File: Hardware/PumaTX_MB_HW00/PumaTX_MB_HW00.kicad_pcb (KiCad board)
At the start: 4 copper layers, 130 x 40 mm, 115 parts, among them J100 FH12A-26S-0.5SH_55_, J101 FH12-12S-0.5SH_55_, J102 500334-0160, J103 500334-0160, J104 692122030100, J105 53398-0667, J400 U.FL-R-SMT-1_40_, J410 U.FL-R-SMT-1_40_, M130 Motor_DC, M140 Fan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

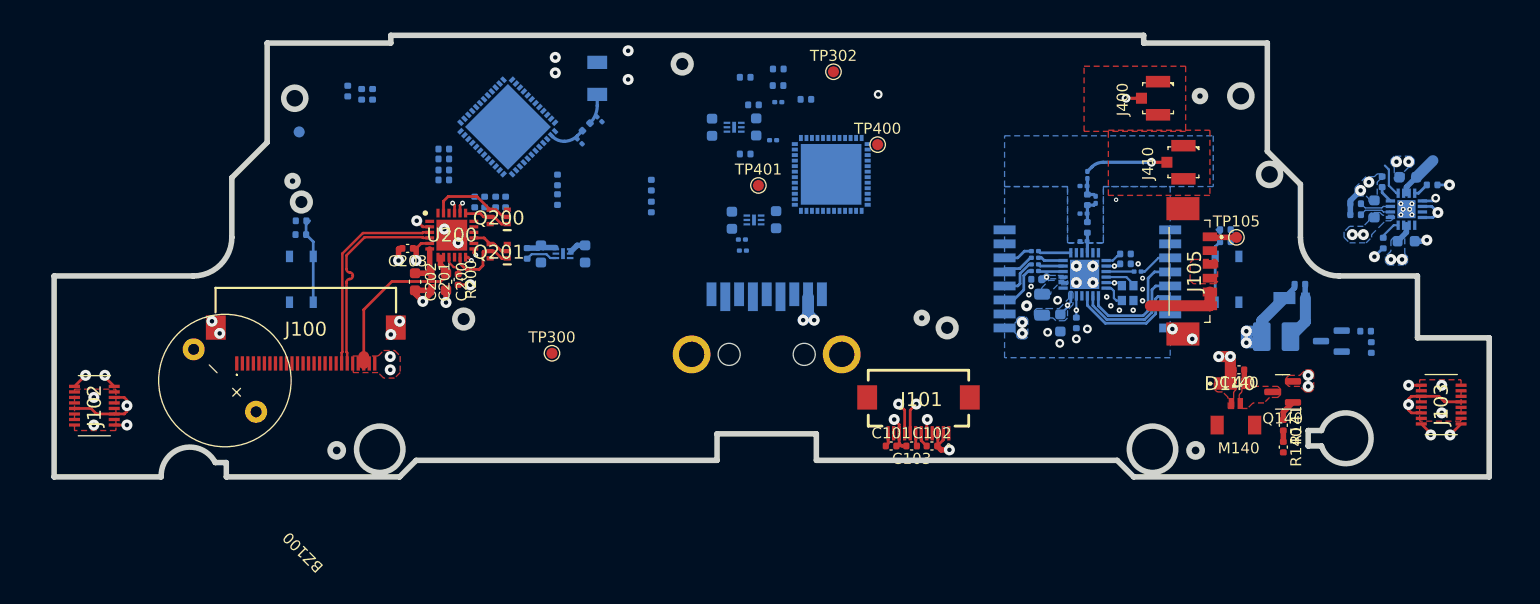
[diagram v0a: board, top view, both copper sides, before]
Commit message: some changes on routing, every QFN is on the same side
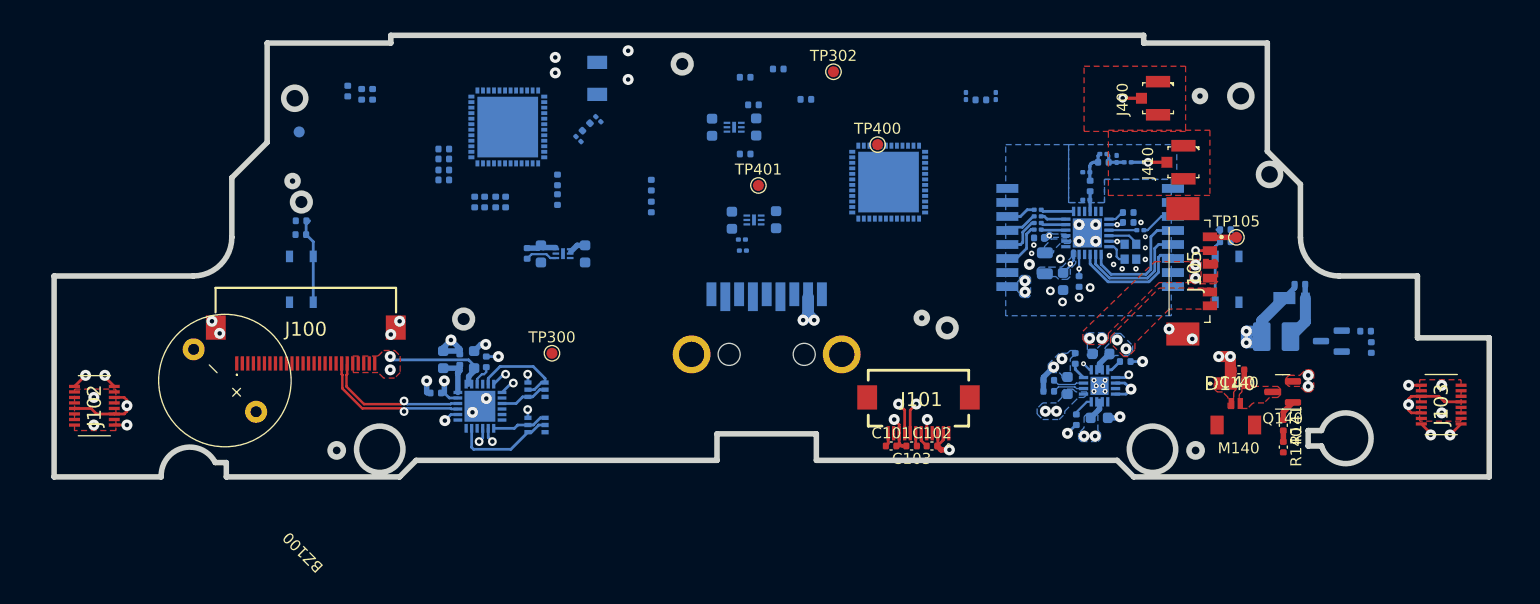
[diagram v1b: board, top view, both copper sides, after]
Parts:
- C200, C201, C202, C203, Q200, Q201, R200, U200: moved to B.Cu
- moved C501 32.1 mm to (173.2, 114.9)
- moved C502 32.1 mm to (176.1, 117.8)
- moved C503 32.1 mm to (176.2, 112.0)
- moved R502 32.1 mm to (174.0, 118.0)
- moved R504 32.1 mm to (171.5, 114.5)
- moved R505 32.1 mm to (171.5, 115.5)
- moved U500 32.1 mm to (176.1, 115.0)
- moved R501 32.1 mm to (178.4, 112.8)
- moved R503 32.1 mm to (173.9, 112.5)
- moved C407 19.7 mm to (166.7, 88.7), turned to 90 degrees
- moved Q200 19.2 mm to (125.1, 118.5)
- moved L400 18.4 mm to (165.3, 89.0)
- moved C406 17.9 mm to (164.0, 88.7), turned to 90 degrees
- moved U200 15.7 mm to (120.0, 116.8)
- moved C203 13.3 mm to (116.0, 115.6)
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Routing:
- net VBUS: track 99.9 -> 14.5 mm
- net /BATTERY_TEMP: track 3.18 -> 21.3 mm, vias 0 -> 2
- net /VBAT: track 10.6 -> 1.87 mm, vias 0 -> 2
- net /VSYS: track 29.3 -> 21.4 mm
- net /D-: track 18.7 -> 13.1 mm, vias 0 -> 1
- net /D+: track 18.7 -> 13.8 mm, vias 0 -> 1
- net /50_ELRS_ANT_4: track 7.48 -> 3.23 mm
- net /50_PUMATX_ANT_1: track 3.31 -> 0.00 mm
- net /50_PUMATX_ANT_2: track 2.95 -> 0.18 mm
- net /ELRS_RTS: track 6.74 -> 8.76 mm
- net /PUMATX_DTR: track 7.79 -> 9.36 mm
- net /ELRS_DTR: track 3.52 -> 4.42 mm
- net /PUMATX_RTS: track 4.17 -> 5.04 mm
- net /TX_ELRS_DEBUG: track 0.65 -> 1.45 mm
- net /ELRS_CHIP_PU: track 0.00 -> 0.76 mm, vias 0 -> 1
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- added copper zone on B.Cu, net /VBAT
- added copper zone on F.Cu, net /VBAT

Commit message: Routing goes on and on and on...
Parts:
- moved C300 20.5 mm to (116.5, 91.0), turned to 180 degrees
- moved R300 20.2 mm to (116.5, 90.0), turned to 0 degrees
- moved C531 17.1 mm to (162.9, 105.4)
- moved C530 17.0 mm to (158.9, 105.4)
- moved U530 17.0 mm to (160.9, 105.4)
- moved R512 13.0 mm to (156.6, 105.1), turned to -90 degrees
- moved R511 12.6 mm to (155.8, 105.1), turned to -90 degrees
- moved C401 12.5 mm to (156.0, 90.5), turned to 90 degrees
- moved C450 12.0 mm to (156.0, 87.0)
- moved C452 11.3 mm to (156.0, 88.0)
- moved C350 9.08 mm to (117.0, 87.0), turned to 90 degrees
- moved C451 9.00 mm to (156.0, 86.0)
- moved R401 7.65 mm to (157.0, 90.5), turned to -90 degrees
- moved U400 7.02 mm to (150.0, 96.0)
- moved C351 6.91 mm to (116.0, 87.0), turned to 90 degrees
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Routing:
- net /MISO: track 4.32 -> 36.7 mm
- net /MOSI: track 3.78 -> 26.7 mm
- net /SCK: track 2.84 -> 25.2 mm
- net /NSS: track 2.68 -> 24.6 mm
- net /RX_EN: track 0.00 -> 15.4 mm
- net /AUX_EN: track 0.00 -> 7.85 mm
- net /TX_EN: track 0.00 -> 2.38 mm, vias 0 -> 1
- net +3V3: track 21.0 -> 22.7 mm, vias 4 -> 7
- net /VSYS: track 21.4 -> 20.1 mm, vias 7 -> 13
- net /3V3_EN: track 2.91 -> 3.97 mm
- net VBUS: track 14.5 -> 15.5 mm
- net /C1: track 7.77 -> 7.02 mm
- net /DIO2: track 10.8 -> 10.4 mm, vias 0 -> 1
- net GND: track 28.6 -> 28.2 mm, vias 62 -> 71
- net /SX1280_3V3: track 1.67 -> 1.71 mm, vias 4 -> 6
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- added copper zone on B.Cu, net +3V3
- added copper zone on B.Cu, net -3V3

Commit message: and on and on and on... It is getting harder
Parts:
- C201: footprint Capacitor_SMD:C_0402_1005Metric -> Capacitor_SMD:C_0603_1608Metric
- TP400: moved to B.Cu
- moved R512 28.8 mm to (130.5, 93.0), turned to 90 degrees
- moved R511 27.4 mm to (131.2, 93.0), turned to 90 degrees
- moved C407 19.1 mm to (147.6, 88.6)
- moved L400 19.1 mm to (146.2, 89.0)
- moved C406 18.6 mm to (145.4, 89.9), turned to 180 degrees
- moved R305 15.4 mm to (119.2, 85.4), turned to -90 degrees
- moved R510 14.9 mm to (139.7, 97.5), turned to -90 degrees
- moved R306 14.3 mm to (120.2, 85.4), turned to 90 degrees
- moved TP302 13.9 mm to (154.2, 100.2)
- moved C450 13.2 mm to (143.3, 90.5), turned to 90 degrees
- moved C510 11.0 mm to (137.4, 97.5), turned to 90 degrees
- moved TP400 10.4 mm to (149.6, 84.9), turned to 180 degrees
- moved C451 10.00 mm to (153.2, 95.6), turned to -90 degrees
- moved U510 8.12 mm to (135.4, 97.6), turned to 0 degrees
- moved C452 8.03 mm to (148.4, 90.6), turned to 0 degrees
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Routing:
- net VBUS: track 15.5 -> 104.5 mm
- net /VSYS: track 20.1 -> 107.9 mm, vias 13 -> 14
- net /50_ESP_ELRS_ANT_2: track 1.40 -> 33.2 mm
- net /MISO: track 36.7 -> 4.92 mm
- net /MOSI: track 26.7 -> 3.78 mm
- net /SCK: track 25.2 -> 2.84 mm
- net /NSS: track 24.6 -> 2.68 mm
- net /RX_EN: track 15.4 -> 0.00 mm
- net /DISPLAY_BACKLIGHT: track 0.00 -> 9.46 mm, vias 0 -> 3
- net -3V3: track 0.00 -> 8.72 mm, vias 2 -> 7
- net /LED: track 0.00 -> 8.50 mm, vias 0 -> 2
- net GND: track 28.2 -> 34.3 mm, vias 71 -> 96
- net /HAPTIC_LS: track 5.31 -> 0.03 mm
- net /RECORD: track 0.00 -> 4.40 mm
- net /BQ_PGOOD: track 0.00 -> 3.33 mm
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- added copper zone on B.Cu, net /HAPTIC_LS
- added copper zone on In1.Cu, net /VSYS

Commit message: Wow its gonna be complicated
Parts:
- added R101: 0k, Capacitor_SMD:C_0402_1005Metric, F.Cu at (123.1, 119.3)
- added R102: 0k, Capacitor_SMD:C_0402_1005Metric, F.Cu at (123.1, 120.2)
- TP301, TP400: moved to F.Cu
- moved C304 50.7 mm to (160.6, 119.7), turned to -90 degrees
- moved R304 50.3 mm to (159.6, 119.7), turned to 90 degrees
- moved R303 49.9 mm to (158.6, 119.7), turned to 90 degrees
- moved C303 49.5 mm to (157.6, 119.7), turned to -90 degrees
- moved TP301 23.9 mm to (126.2, 99.6), turned to 0 degrees
- moved TP302 22.8 mm to (134.0, 89.6)
- moved TP300 21.9 mm to (125.2, 90.2)
- moved C351 15.9 mm to (129.2, 95.8), turned to -90 degrees
- moved R305 12.2 mm to (107.5, 89.0)
- moved R306 12.2 mm to (108.5, 89.0)
- moved TP400 11.5 mm to (157.8, 92.9), turned to 0 degrees
- moved ANT300 7.33 mm to (123.4, 85.7), turned to 0 degrees
- moved TP401 5.77 mm to (150.2, 99.6)
- moved C307 5.77 mm to (121.4, 87.4), turned to 180 degrees
- moved L300 4.70 mm to (121.7, 88.8), turned to -90 degrees
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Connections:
- J104 pad 1: VBUS -> /VSYS
- J104 pad 2: /VSYS -> VBUS
- J104 pad 5: /TX_PUMATX_DEBUG -> Net-(J104-Pad5)
- J104 pad 6: /RX_PUMATX_DEBUG -> Net-(J104-Pad6)
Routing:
- net /CRSF: track 0.00 -> 46.3 mm, vias 0 -> 4
- net /DIO2: track 10.4 -> 44.3 mm, vias 1 -> 2
- net Net-(J104-Pad5): track 0.00 -> 33.4 mm, vias 0 -> 1
- net /DIO1: track 10.9 -> 43.9 mm, vias 1 -> 2
- net Net-(J104-Pad6): track 0.00 -> 32.6 mm, vias 0 -> 1
- net /MISO: track 4.92 -> 35.1 mm
- net /TX_PUMATX_DEBUG: track 1.36 -> 31.0 mm, vias 1 -> 2
- net /RX_PUMATX_DEBUG: track 1.33 -> 30.9 mm, vias 1 -> 2
- net /RX_ELRS_DEBUG: track 3.08 -> 31.5 mm
- net /TX_ELRS_DEBUG: track 3.65 -> 31.9 mm
- net /MOSI: track 3.78 -> 28.5 mm
- net /SCK: track 2.84 -> 26.4 mm
- net /NSS: track 2.68 -> 25.5 mm
- net /DISPLAY_SDA: track 2.88 -> 25.1 mm, vias 0 -> 1
- net /DISPLAY_SCL: track 2.98 -> 23.7 mm, vias 0 -> 1
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
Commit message: Almost done !! only 3 PSU to go
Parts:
- added J100: FH12A-26S-0.5SH_55_, Component_lib:FH12A26S05SH55, F.Cu at (104.2, 109.5)
- C300, C301, C302, R305, R306: moved to F.Cu
- R300, R301, R302: footprint Capacitor_SMD:C_0402_1005Metric -> Capacitor_SMD:C_0201_0603Metric; moved to F.Cu
- R303, R304, R401: footprint Capacitor_SMD:C_0402_1005Metric -> Capacitor_SMD:C_0201_0603Metric
- moved R305 23.7 mm to (128.2, 100.5), turned to 90 degrees
- moved R306 22.0 mm to (127.2, 100.5), turned to -90 degrees
- moved C301 14.1 mm to (129.1, 91.5), turned to 90 degrees
- moved R301 13.9 mm to (129.8, 91.5), turned to -90 degrees
- moved C300 11.4 mm to (127.8, 89.2), turned to 0 degrees
- moved R300 11.4 mm to (127.8, 88.4), turned to 180 degrees
- moved R302 11.0 mm to (129.8, 94.3)
- moved C302 10.1 mm to (129.1, 94.3)
- moved C352 4.20 mm to (111.2, 88.9)
- moved C350 4.20 mm to (113.2, 88.9)
- moved ANT300 3.15 mm to (120.2, 85.7), turned to 180 degrees
- moved TP300 0.96 mm to (125.7, 89.3)
- moved D130 0.92 mm to (192.7, 107.0)
- moved C130 0.86 mm to (193.2, 105.8)
- moved TP301 0.56 mm to (125.8, 99.3)
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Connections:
- U300 pad 11: /LEFT_POT -> /C2
- U300 pad 14: /PUMATX_SCL -> /PUMATX_SDA
- U300 pad 15: /PUMATX_SDA -> /PUMATX_SCL
- U300 pad 21: /RECORD -> /PAUSE
- U300 pad 25: /OK -> /RTH
- U300 pad 34: /PAUSE -> /UP
- U300 pad 35: /RTH -> /OK
- U300 pad 36: /PHOTO -> /C1
- U300 pad 38: /C2 -> /LEFT
- U300 pad 39: /C1 -> /RIGHT
- U300 pad 5: /RIGHT -> /LEFT_POT
- U300 pad 6: /LEFT -> /PHOTO
- U300 pad 7: /UP -> /RECORD
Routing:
- net /PUMATX_SDA: track 2.83 -> 181.8 mm, vias 2 -> 4
- net /PUMATX_SCL: track 2.70 -> 178.9 mm, vias 2 -> 4
- net /SPORT: track 0.00 -> 109.2 mm, vias 0 -> 6
- net /RIGHT_POT: track 1.15 -> 110.3 mm, vias 1 -> 2
- net /HAPTIC_PWM: track 1.80 -> 92.9 mm, vias 0 -> 2
- net /C2: track 6.88 -> 96.5 mm
- net /BUZZER_PWM: track 0.00 -> 70.5 mm, vias 0 -> 2
- net /FAN_PWM: track 1.02 -> 63.5 mm, vias 0 -> 5
- net /LEFT_POT: track 1.15 -> 62.3 mm, vias 1 -> 3
- net /VBAT: track 1.87 -> 57.3 mm, vias 2 -> 5
- net /DISPLAY_BACKLIGHT: track 9.17 -> 58.0 mm, vias 3 -> 4
- net /ELRS_CHIP_PU: track 11.4 -> 59.1 mm, vias 2 -> 6
- net /PHOTO: track 0.00 -> 43.7 mm, vias 0 -> 2
- net /AUX_EN: track 9.00 -> 51.6 mm
- net /ON_OFF: track 0.00 -> 42.5 mm, vias 0 -> 2
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
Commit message: Is this the end? or is it just the beginning?
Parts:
- added G***: LOGO, Component_lib:puma_logo_14mm, F.Cu at (166.0, 100.2)
- added TP501: BQ_PGOOD, TestPoint:TestPoint_Pad_D1.0mm, B.Cu at (181.0, 114.6)
- added TP502: BQ_CHG, TestPoint:TestPoint_Pad_D1.0mm, B.Cu at (178.0, 117.0)
- moved C352 12.1 mm to (123.3, 89.4), turned to 0 degrees
- moved C350 6.26 mm to (119.4, 90.1)
- moved C302 0.10 mm to (129.1, 94.2)
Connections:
- M140 pad 3: (no net) -> GND
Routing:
- net +3V3: track 43.4 -> 293.3 mm, vias 15 -> 20
- net GND: track 80.8 -> 106.1 mm, vias 116 -> 123
- net -3V3: track 19.2 -> 44.3 mm, vias 9 -> 7
- net /SX1280_3V3: track 1.71 -> 19.0 mm
- net /DISPLAY_SCL: track 58.1 -> 62.8 mm
- net /FAN_PWM: track 63.5 -> 62.8 mm
- net /VSYS: track 107.3 -> 106.6 mm
- net /RIGHT_POT: vias 2 -> 1
- net /LEFT_POT: vias 3 -> 2
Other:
- board text added: "PUMA"
- board text added: "PumaTX_MB_HW00"
- board text added: "TX"
